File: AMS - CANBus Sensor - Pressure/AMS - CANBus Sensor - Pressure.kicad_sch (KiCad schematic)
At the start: 10 parts, among them J3 Conn_02x10_Odd_Even, J5 Power_And_CAN, Q1 IRF9Z34NPBF, U2 178.6165.0001

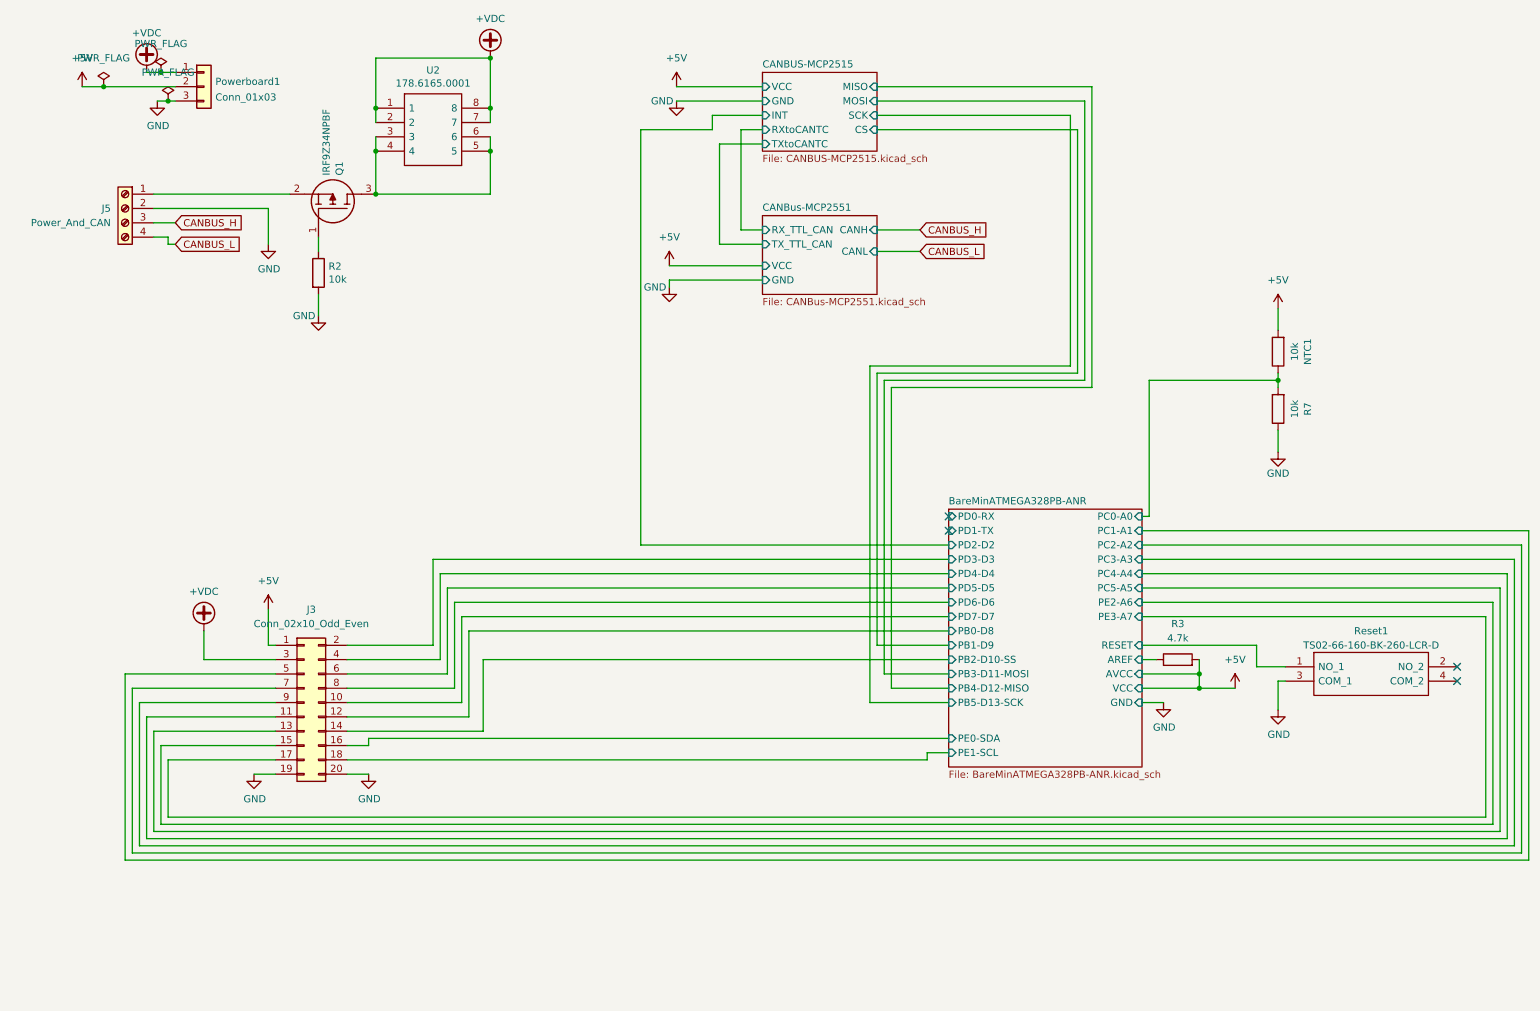
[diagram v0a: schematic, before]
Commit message: working on the SMD version Making The Pressure version based off of the DIP Package
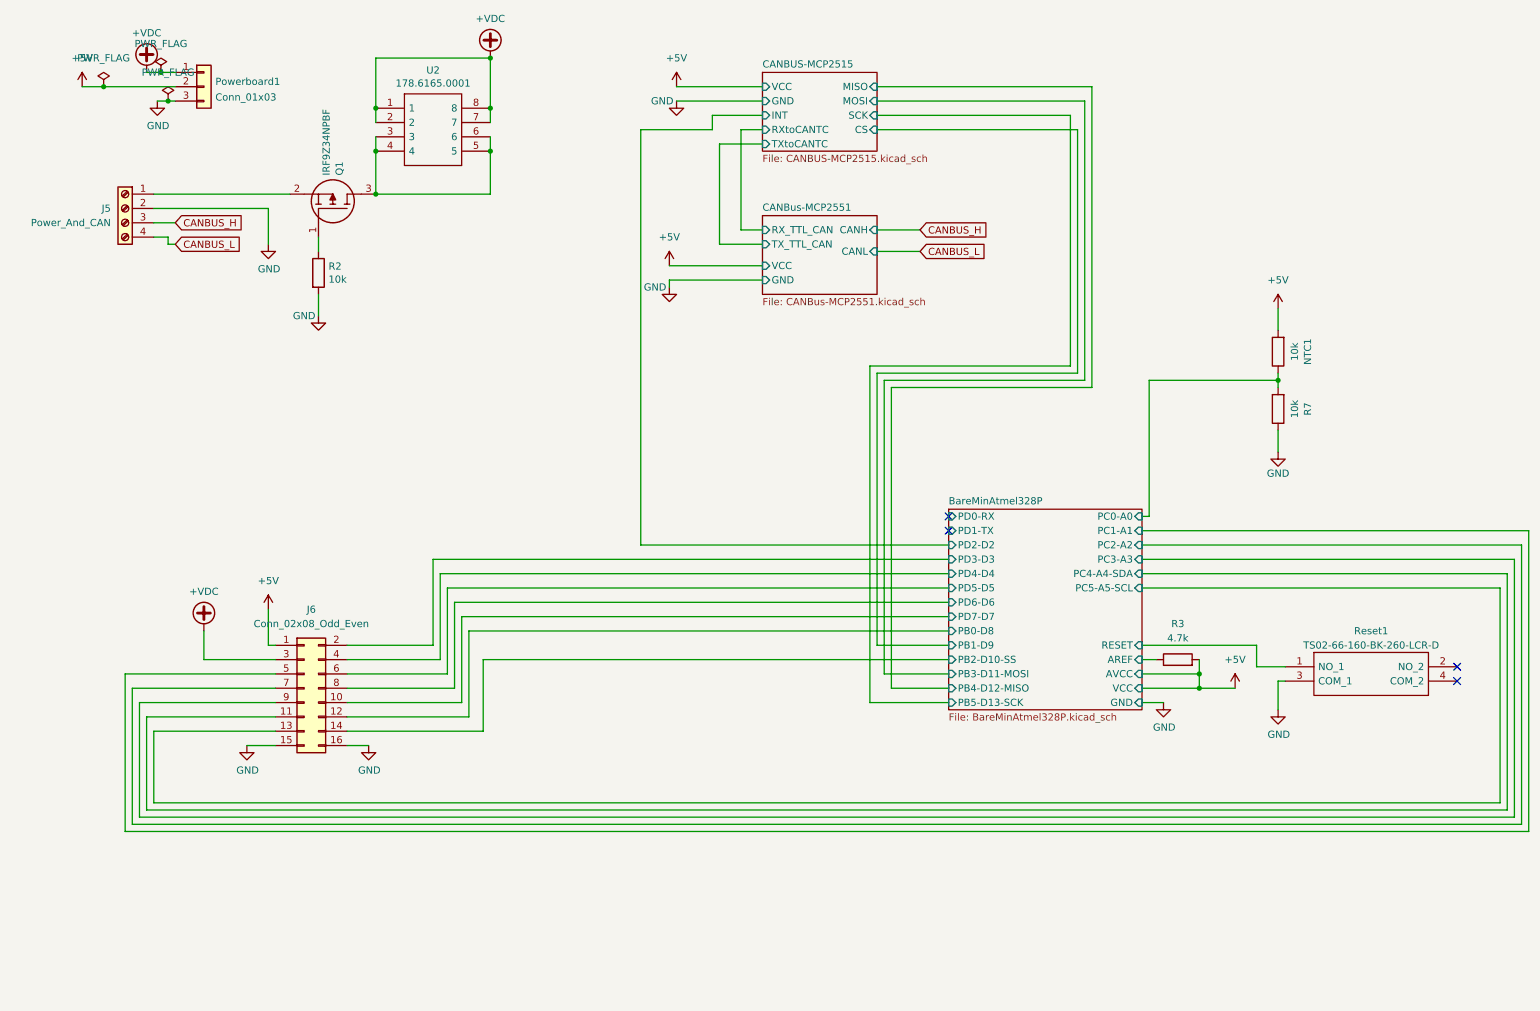
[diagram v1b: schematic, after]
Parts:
- removed J3: Conn_02x10_Odd_Even, Connector_PinHeader_2.54mm:PinHeader_2x10_P2.54mm_Vertical, symbol Connector_Generic:Conn_02x10_Odd_Even
- added J6: Conn_02x08_Odd_Even, Connector_PinHeader_2.54mm:PinHeader_2x08_P2.54mm_Vertical, symbol Connector_Generic:Conn_02x08_Odd_Even
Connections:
- net +5V: now also J6.1 (Pin_1)
- net +VDC: now also J6.3 (Pin_3)
- net BareMinAtmel328P/PB0-D8: now also J6.12 (Pin_12)
- net BareMinAtmel328P/PB2-D10-SS: now also J6.14 (Pin_14)
- net BareMinAtmel328P/PC1-A1: now also J6.5 (Pin_5)
- net BareMinAtmel328P/PC2-A2: now also J6.7 (Pin_7)
- net BareMinAtmel328P/PC3-A3: now also J6.9 (Pin_9)
- net BareMinAtmel328P/PD3-D3: now also J6.2 (Pin_2)
- net BareMinAtmel328P/PD4-D4: now also J6.4 (Pin_4)
- net BareMinAtmel328P/PD5-D5: now also J6.6 (Pin_6)
- net BareMinAtmel328P/PD6-D6: now also J6.8 (Pin_8)
- net BareMinAtmel328P/PD7-D7: now also J6.10 (Pin_10)
- net GND: now also J6.15 (Pin_15), J6.16 (Pin_16)
- new net BareMinAtmel328P/PC4-A4-SDA: J6.11 (Pin_11)
- new net BareMinAtmel328P/PC5-A5-SCL: J6.13 (Pin_13)
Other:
- sheet BareMinATMEGA328PB-ANR renamed BareMinAtmel328P
- sheet BareMinAtmel328P: file BareMinATMEGA328PB-ANR.kicad_sch -> BareMinAtmel328P.kicad_sch
- sheet BareMinAtmel328P ports: added PC4-A4-SDA, PC5-A5-SCL; removed PC4-A4, PC5-A5, PE0-SDA, PE1-SCL, PE2-A6, PE3-A7

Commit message: wip for this trying to figure out if i want to go completely SMD with this or not.
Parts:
- removed J6: Conn_02x08_Odd_Even, Connector_PinHeader_2.54mm:PinHeader_2x08_P2.54mm_Vertical, symbol Connector_Generic:Conn_02x08_Odd_Even
- removed U2: 178.6165.0001, SamacSys_Parts:17861650001, symbol SamacSys_Parts:178.6165.0001
- added J2: Power_And_CAN, TerminalBlock_Phoenix:TerminalBlock_Phoenix_MPT-0,5-4-2.54_1x04_P2.54mm_Horizontal, symbol Connector:Screw_Terminal_01x04
- added J6: Screw_Terminal_01x02, TerminalBlock_Phoenix:TerminalBlock_Phoenix_MPT-0,5-2-2.54_1x02_P2.54mm_Horizontal, symbol Connector:Screw_Terminal_01x02
- added RV1, RV2, RV3, RV4: R_Potentiometer_US, Potentiometer_THT:Potentiometer_Bourns_3296W_Vertical, symbol Device:R_Potentiometer_US
- added U1, U5: 3568, 3568, symbol SamacSys_Parts:3568
- renumbered J5 to J1, R2 to R1, R3 to R2, R7 to R3
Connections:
- net +5V: now also U1.3, U1.4
- net +VDC: now also U5.3, U5.4
- net BareMinAtmel328P/PD3-D3: now also J6.1 (Pin_1), J6.2 (Pin_2), U1.1, U1.2
- net GND: now also RV1.3, RV2.3, RV3.3, RV4.3
- net at Q1.3: now also U5.1, U5.2
- new net: J2.1 (Pin_1), RV4.1
- new net: J2.2 (Pin_2), RV3.1
- new net: J2.3 (Pin_3), RV2.1
- new net: J2.4 (Pin_4), RV1.1
- new net BufferedADC/ADCIN1: RV4.2
- new net BufferedADC/ADCIN2: RV3.2
- new net BufferedADC/ADCIN3: RV2.2
- new net BufferedADC/ADCIN4: RV1.2
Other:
- added sheet BufferedADC (BufferedADC.kicad_sch)

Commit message: ready for fab
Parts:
- Q1: footprint SamacSys_Parts:TO254P469X1042X1967-3P -> TO254P469X1042X1967-3P; Mouser Price/Stock https://www.mouser.co.uk/ProductDetail/Infineon-IR/IRF9Z34N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 -> https://www.mouser.co.uk/ProductDetail/Infineon-Technologie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
- RV1, RV2, RV3, RV4: value R_Potentiometer_US -> 200k
- Reset1: footprint SamacSys_Parts:TS0266160BK260LCRD -> TS0266160BK260LCRD
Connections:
- net BareMinAtmel328P/PD3-D3: no longer J6.1 (Pin_1), J6.2 (Pin_2), U1.1, U1.2
- net BufferedADC/ADCIN1: now also RV1.2; no longer RV4.2
- net BufferedADC/ADCIN2: now also RV2.2; no longer RV3.2
- net BufferedADC/ADCIN3: now also RV3.2; no longer RV2.2
- net BufferedADC/ADCIN4: now also RV4.2; no longer RV1.2
- net at RV4.1: now also J2.4 (Pin_4); no longer J2.1 (Pin_1)
- net at J2.2 (Pin_2): now also RV2.1; no longer RV3.1
- net at J2.3 (Pin_3): now also RV3.1; no longer RV2.1
- net at RV1.1: now also J2.1 (Pin_1); no longer J2.4 (Pin_4)
- new net: J6.2 (Pin_2), U1.1
- new net: J6.1 (Pin_1), U1.2
- no-connect marks 4 -> 12
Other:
- moved on the sheet: RV1, RV2, RV3, RV4

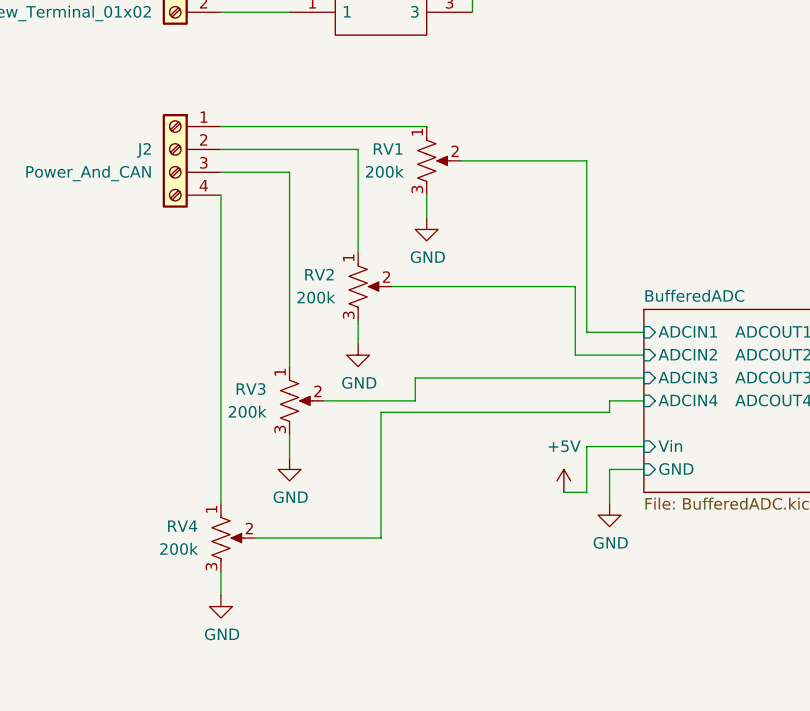
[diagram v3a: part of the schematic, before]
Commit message: removed un-needed BufferedADC.kicad_sch from IO and Temp boards as that was copied over.
R8,9,14,15 100k resistors were removed from the ADC input and in parallel witht he 200k pots and then moved to be in series with the pots and changed to 1k
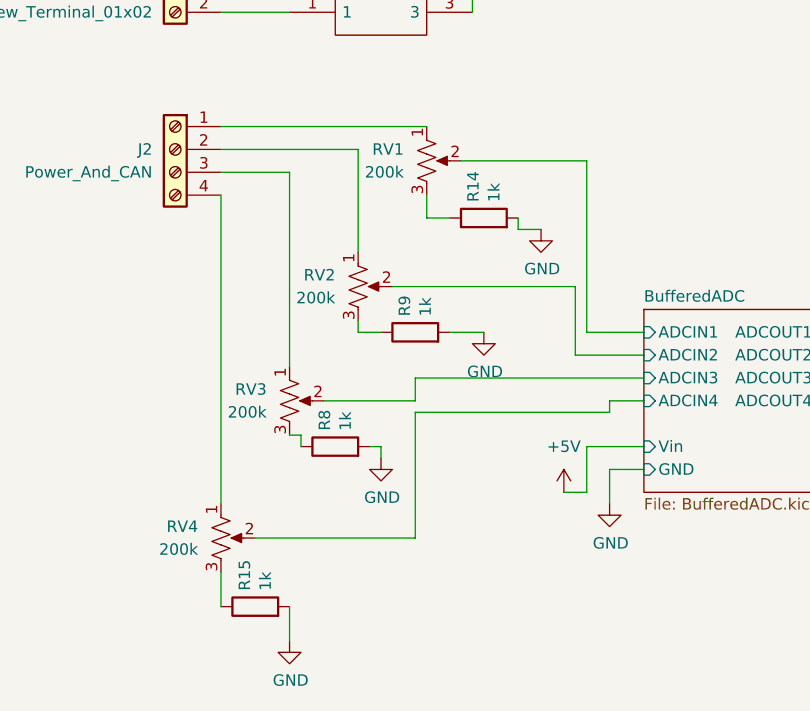
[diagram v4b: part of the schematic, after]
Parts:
- added R14, R15, R8, R9: 1k, Resistor_SMD:R_1206_3216Metric_Pad1.30x1.75mm_HandSolder, symbol Device:R
- J6: footprint TerminalBlock_Phoenix:TerminalBlock_Phoenix_MPT-0,5-2-2.54_1x02_P2.54mm_Horizontal -> TerminalBlock_TE-Connectivity:TerminalBlock_TE_282834-2_1x02_P2.54mm_Horizontal
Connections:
- net GND: now also R14.2, R15.2, R8.2, R9.2; no longer RV1.3, RV2.3, RV3.3, RV4.3
- new net: R15.1, RV4.3
- new net: R14.1, RV1.3
- new net: R8.1, RV3.3
- new net: R9.1, RV2.3
